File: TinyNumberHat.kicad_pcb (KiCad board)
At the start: 4 copper layers, 65 x 30 mm, 38 parts, among them IC1 SamacSys_Parts_HT16K33-28SOP, J1 GPIO, J2 SM04B-SRSS-TB(LF)(SN), SW1 SW_Omron_B3FS, SW2 SW_Omron_B3FS, SW3 SW_Omron_B3FS, SW4 SW_Omron_B3FS

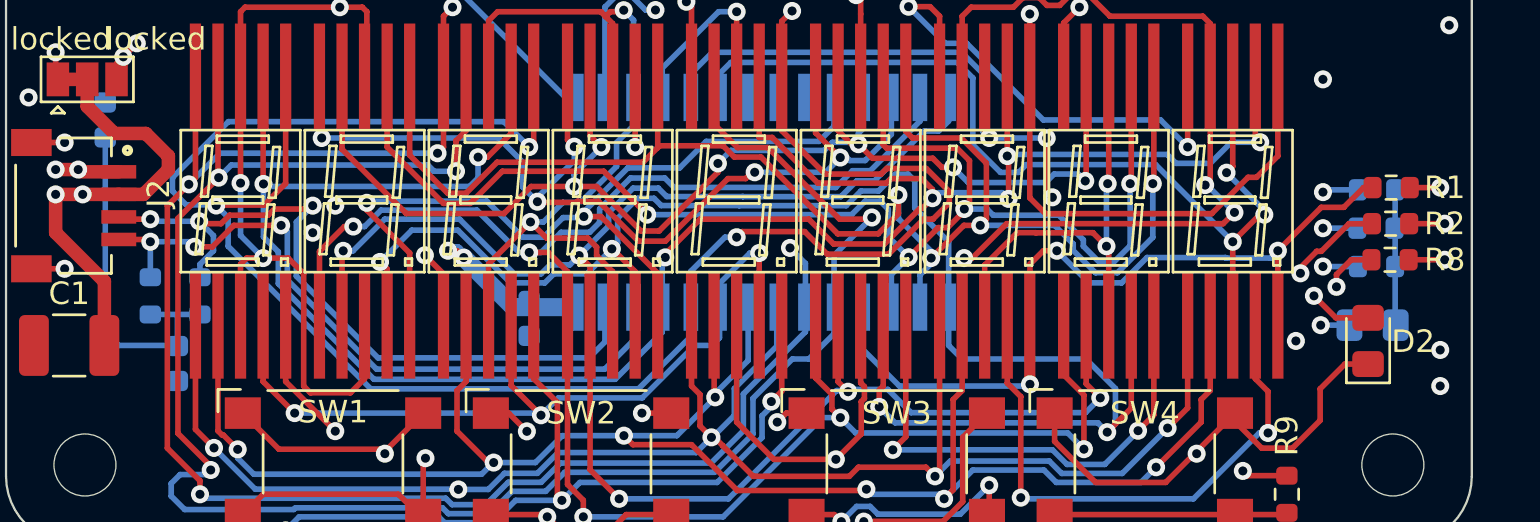
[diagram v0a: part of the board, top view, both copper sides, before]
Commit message: Update silkscreens
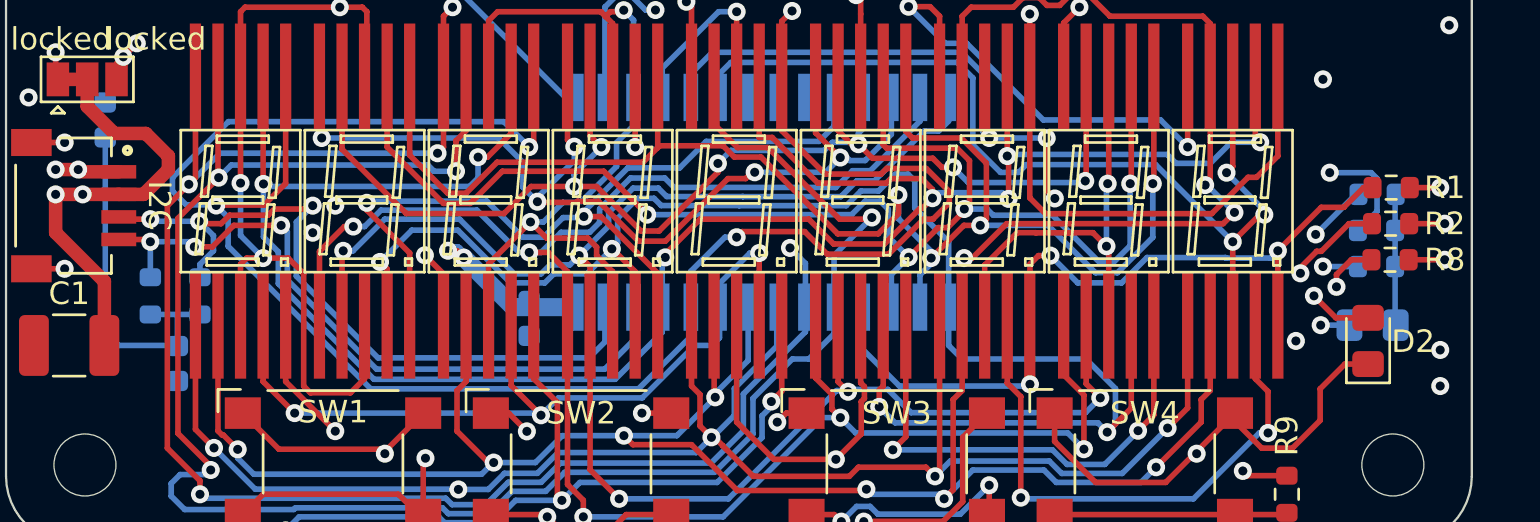
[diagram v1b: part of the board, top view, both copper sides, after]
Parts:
- moved R4 1.80 mm to (160.8, 86.1)
- moved R5 1.50 mm to (160.8, 84.5)
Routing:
- net /an1: track 143.2 -> 146.2 mm
- net /an2: track 97.4 -> 98.1 mm

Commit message: Minor updates
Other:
- board text removed: "Extend PCB edge 0.5mm if using SMT header"
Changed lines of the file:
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@@
     )
   )
-  (footprint "Button_Switch_SMD:SW_SPST_Omron_B3FS-105xP" (layer "F.Cu")
+  (footprint "Button_Switch_SMD:SW_SPST_Omron_B3FS-105xP" locked (layer "F.Cu")
     (at 150.5 96.45)
     (descr "Surface Mount Tactile Switch for High-Density Mounting, 7.3mm height, https://omronfs.omron.com/en_US/ecb/products/pdf/en-b3fs.pdf")
@@
     (fp_circle (center 0 0) (end 1.5 0)
       (stroke (width 0.1) (type solid)) (fill none) (layer "F.Fab"))
-    (pad "1" smd rect (at -4 -2.25 180) (size 1.6 1.4) (layers "F.Cu" "F.Paste" "F.Mask")
+    (pad "1" smd rect locked (at -4 -2.25 180) (size 1.6 1.4) (layers "F.Cu" "F.Paste" "F.Mask")
       (net 32 "Net-(D2-K)") (pinfunction "1") (pintype "passive"))
-    (pad "1" smd rect (at 4 -2.25 180) (size 1.6 1.4) (layers "F.Cu" "F.Paste" "F.Mask")
+    (pad "1" smd rect locked (at 4 -2.25 180) (size 1.6 1.4) (layers "F.Cu" "F.Paste" "F.Mask")
       (net 32 "Net-(D2-K)") (pinfunction "1") (pintype "passive"))
-    (pad "2" smd rect (at -4 2.25 180) (size 1.6 1.4) (layers "F.Cu" "F.Paste" "F.Mask")
+    (pad "2" smd rect locked (at -4 2.25 180) (size 1.6 1.4) (layers "F.Cu" "F.Paste" "F.Mask")
       (net 61 "Net-(R9-Pad1)") (pinfunction "2") (pintype "passive"))
-    (pad "2" smd rect (at 4 2.25 180) (size 1.6 1.4) (layers "F.Cu" "F.Paste" "F.Mask")
+    (pad "2" smd rect locked (at 4 2.25 180) (size 1.6 1.4) (layers "F.Cu" "F.Paste" "F.Mask")
       (net 61 "Net-(R9-Pad1)") (pinfunction "2") (pintype "passive"))
     (model "${KICAD6_3DMODEL_DIR}/Button_Switch_SMD.3dshapes/SW_SPST_Omron_B3FS-105xP.wrl"
@@
     )
   )
-  (footprint "Button_Switch_SMD:SW_SPST_Omron_B3FS-105xP" (layer "F.Cu")
+  (footprint "Button_Switch_SMD:SW_SPST_Omron_B3FS-105xP" locked (layer "F.Cu")
     (at 114.5 96.45)
     (descr "Surface Mount Tactile Switch for High-Density Mounting, 7.3mm height, https://omronfs.omron.com/en_US/ecb/products/pdf/en-b3fs.pdf")
@@
     (fp_circle (center 0 0) (end 1.5 0)
       (stroke (width 0.1) (type solid)) (fill none) (layer "F.Fab"))
-    (pad "1" smd rect (at -4 -2.25 180) (size 1.6 1.4) (layers "F.Cu" "F.Paste" "F.Mask")
+    (pad "1" smd rect locked (at -4 -2.25 180) (size 1.6 1.4) (layers "F.Cu" "F.Paste" "F.Mask")
       (net 32 "Net-(D2-K)") (pinfunction "1") (pintype "passive"))
-    (pad "1" smd rect (at 4 -2.25 180) (size 1.6 1.4) (layers "F.Cu" "F.Paste" "F.Mask")
+    (pad "1" smd rect locked (at 4 -2.25 180) (size 1.6 1.4) (layers "F.Cu" "F.Paste" "F.Mask")
       (net 32 "Net-(D2-K)") (pinfunction "1") (pintype "passive"))
-    (pad "2" smd rect (at -4 2.25 180) (size 1.6 1.4) (layers "F.Cu" "F.Paste" "F.Mask")
+    (pad "2" smd rect locked (at -4 2.25 180) (size 1.6 1.4) (layers "F.Cu" "F.Paste" "F.Mask")
       (net 33 "Net-(R1-Pad1)") (pinfunction "2") (pintype "passive"))
-    (pad "2" smd rect (at 4 2.25 180) (size 1.6 1.4) (layers "F.Cu" "F.Paste" "F.Mask")
+    (pad "2" smd rect locked (at 4 2.25 180) (size 1.6 1.4) (layers "F.Cu" "F.Paste" "F.Mask")
       (net 33 "Net-(R1-Pad1)") (pinfunction "2") (pintype "passive"))
     (model "${KICAD6_3DMODEL_DIR}/Button_Switch_SMD.3dshapes/SW_SPST_Omron_B3FS-105xP.wrl"
@@
     )
   )
-  (footprint "Button_Switch_SMD:SW_SPST_Omron_B3FS-105xP" (layer "F.Cu")
+  (footprint "Button_Switch_SMD:SW_SPST_Omron_B3FS-105xP" locked (layer "F.Cu")
     (at 125.5 96.45)
     (descr "Surface Mount Tactile Switch for High-Density Mounting, 7.3mm height, https://omronfs.omron.com/en_US/ecb/products/pdf/en-b3fs.pdf")
@@
     (fp_circle (center 0 0) (end 1.5 0)
       (stroke (width 0.1) (type solid)) (fill none) (layer "F.Fab"))
-    (pad "1" smd rect (at -4 -2.25 180) (size 1.6 1.4) (layers "F.Cu" "F.Paste" "F.Mask")
+    (pad "1" smd rect locked (at -4 -2.25 180) (size 1.6 1.4) (layers "F.Cu" "F.Paste" "F.Mask")
       (net 32 "Net-(D2-K)") (pinfunction "1") (pintype "passive"))
-    (pad "1" smd rect (at 4 -2.25 180) (size 1.6 1.4) (layers "F.Cu" "F.Paste" "F.Mask")
+    (pad "1" smd rect locked (at 4 -2.25 180) (size 1.6 1.4) (layers "F.Cu" "F.Paste" "F.Mask")
       (net 32 "Net-(D2-K)") (pinfunction "1") (pintype "passive"))
-    (pad "2" smd rect (at -4 2.25 180) (size 1.6 1.4) (layers "F.Cu" "F.Paste" "F.Mask")
+    (pad "2" smd rect locked (at -4 2.25 180) (size 1.6 1.4) (layers "F.Cu" "F.Paste" "F.Mask")
       (net 34 "Net-(R2-Pad1)") (pinfunction "2") (pintype "passive"))
-    (pad "2" smd rect (at 4 2.25 180) (size 1.6 1.4) (layers "F.Cu" "F.Paste" "F.Mask")
+    (pad "2" smd rect locked (at 4 2.25 180) (size 1.6 1.4) (layers "F.Cu" "F.Paste" "F.Mask")
       (net 34 "Net-(R2-Pad1)") (pinfunction "2") (pintype "passive"))
     (model "${KICAD6_3DMODEL_DIR}/Button_Switch_SMD.3dshapes/SW_SPST_Omron_B3FS-105xP.wrl"
@@
     (effects (font (size 1 1) (thickness 0.15)) (justify left bottom))
   )
-  (gr_text "Extend PCB edge 0.5mm if using SMT header" (at 103 68.5) (layer "Dwgs.User")
-    (effects (font (size 1 1) (thickness 0.15)) (justify left))
-  )
   (gr_text "PoE" (at 161.5 79.64) (layer "Dwgs.User")

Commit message: Small updates
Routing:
- net /an5: track 123.9 -> 131.1 mm
- net /an13: track 61.5 -> 58.8 mm
- net /an1: track 146.2 -> 145.1 mm
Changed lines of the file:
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@@
   (via (at 145.4 76.5) (size 0.8) (drill 0.4) (layers "F.Cu" "B.Cu") (net 38))
   (via (at 132.4 86.4) (size 0.8) (drill 0.4) (layers "F.Cu" "B.Cu") (net 38))
-  (segment (start 137.845403 77.4) (end 135.889999 77.4) (width 0.25) (layer "In1.Cu") (net 38))
   (segment (start 156.362079 81.2) (end 150.1 81.2) (width 0.25) (layer "In1.Cu") (net 38))
   (segment (start 158.7 83.537921) (end 156.362079 81.2) (width 0.25) (layer "In1.Cu") (net 38))
-  (segment (start 145.4 76.5) (end 141.3 76.5) (width 0.25) (layer "In1.Cu") (net 38))
-  (segment (start 139.858434 75.386969) (end 137.845403 77.4) (width 0.25) (layer "In1.Cu") (net 38))
-  (segment (start 135.889999 77.4) (end 134.857326 76.367327) (width 0.25) (layer "In1.Cu") (net 38))
-  (segment (start 141.3 76.5) (end 140.186969 75.386969) (width 0.25) (layer "In1.Cu") (net 38))
-  (segment (start 140.186969 75.386969) (end 139.858434 75.386969) (width 0.25) (layer "In1.Cu") (net 38))
+  (segment (start 144.7 77.2) (end 135.689999 77.2) (width 0.25) (layer "In1.Cu") (net 38))
+  (segment (start 135.689999 77.2) (end 134.857326 76.367327) (width 0.25) (layer "In1.Cu") (net 38))
+  (segment (start 145.4 76.5) (end 144.7 77.2) (width 0.25) (layer "In1.Cu") (net 38))
   (segment (start 150.1 81.2) (end 145.4 76.5) (width 0.25) (layer "In1.Cu") (net 38))
   (segment (start 160.8 83.8) (end 160.8 85.25) (width 0.25) (layer "B.Cu") (net 38))
@@
   (segment (start 153.4 83.863381) (end 153.175467 84.087914) (width 0.25) (layer "F.Cu") (net 44))
   (segment (start 153.975 85.8) (end 154.475 85.3) (width 0.25) (layer "F.Cu") (net 44))
-  (segment (start 147.320405 75.525) (end 147.879595 75.525) (width 0.25) (layer "F.Cu") (net 44))
+  (segment (start 146.639946 76.6) (end 153.075 76.6) (width 0.25) (layer "F.Cu") (net 44))
   (segment (start 138.395443 85.525907) (end 138.32135 85.6) (width 0.25) (layer "F.Cu") (net 44))
-  (segment (start 145.099695 75.775) (end 145.814946 75.775) (width 0.25) (layer "F.Cu") (net 44))
-  (segment (start 142.4 79.3) (end 142.4 76.6) (width 0.25) (layer "F.Cu") (net 44))
+  (segment (start 144.674695 76.2) (end 145.099695 75.775) (width 0.25) (layer "F.Cu") (net 44))
   (segment (start 136.963604 85.6) (end 133.788604 82.425) (width 0.25) (layer "F.Cu") (net 44))
   (segment (start 120.4 81.675) (end 119.954623 82.120377) (width 0.25) (layer "F.Cu") (net 44))
-  (segment (start 153.4 76.925) (end 153.4 79.3) (width 0.25) (layer "F.Cu") (net 44))
   (segment (start 144.37245 85.8) (end 153.975 85.8) (width 0.25) (layer "F.Cu") (net 44))
-  (segment (start 146.160351 76.120405) (end 146.725 76.120405) (width 0.25) (layer "F.Cu") (net 44))
-  (segment (start 148.954595 76.6) (end 153.075 76.6) (width 0.25) (layer "F.Cu") (net 44))
-  (segment (start 145.814946 75.775) (end 146.160351 76.120405) (width 0.25) (layer "F.Cu") (net 44))
+  (segment (start 153.075 76.6) (end 153.4 76.925) (width 0.25) (layer "F.Cu") (net 44))
+  (segment (start 145.099695 75.775) (end 145.814946 75.775) (width 0.25) (layer "F.Cu") (net 44))
   (segment (start 142.8 76.2) (end 144.674695 76.2) (width 0.25) (layer "F.Cu") (net 44))
   (segment (start 131.4 81.38462) (end 131.4 79.3) (width 0.25) (layer "F.Cu") (net 44))
@@
   (segment (start 138.32135 85.6) (end 136.963604 85.6) (width 0.25) (layer "F.Cu") (net 44))
   (segment (start 119.954623 82.120377) (end 119.954623 83.475) (width 0.25) (layer "F.Cu") (net 44))
+  (segment (start 142.4 76.6) (end 142.8 76.2) (width 0.25) (layer "F.Cu") (net 44))
   (segment (start 142.84745 87.325) (end 144.37245 85.8) (width 0.25) (layer "F.Cu") (net 44))
   (segment (start 142.486661 87.325) (end 142.84745 87.325) (width 0.25) (layer "F.Cu") (net 44))
-  (segment (start 147.879595 75.525) (end 148.954595 76.6) (width 0.25) (layer "F.Cu") (net 44))
-  (segment (start 153.075 76.6) (end 153.4 76.925) (width 0.25) (layer "F.Cu") (net 44))
   (segment (start 120.4 79.3) (end 120.4 81.675) (width 0.25) (layer "F.Cu") (net 44))
   (segment (start 107.624062 95.099122) (end 109.077298 96.552358) (width 0.25) (layer "F.Cu") (net 44))
@@
   (segment (start 109.4 83.72762) (end 109.429853 83.757473) (width 0.25) (layer "F.Cu") (net 44))
   (segment (start 132.44038 82.425) (end 131.4 81.38462) (width 0.25) (layer "F.Cu") (net 44))
-  (segment (start 146.725 76.120405) (end 147.320405 75.525) (width 0.25) (layer "F.Cu") (net 44))
-  (segment (start 142.4 76.6) (end 142.8 76.2) (width 0.25) (layer "F.Cu") (net 44))
+  (segment (start 145.814946 75.775) (end 146.639946 76.6) (width 0.25) (layer "F.Cu") (net 44))
+  (segment (start 142.4 79.3) (end 142.4 76.6) (width 0.25) (layer "F.Cu") (net 44))
   (segment (start 107.624062 85.563264) (end 107.624062 95.099122) (width 0.25) (layer "F.Cu") (net 44))
   (segment (start 133.788604 82.425) (end 132.44038 82.425) (width 0.25) (layer "F.Cu") (net 44))
-  (segment (start 144.674695 76.2) (end 145.099695 75.775) (width 0.25) (layer "F.Cu") (net 44))
   (segment (start 109.429853 83.757473) (end 107.624062 85.563264) (width 0.25) (layer "F.Cu") (net 44))
   (segment (start 109.4 79.3) (end 109.4 83.72762) (width 0.25) (layer "F.Cu") (net 44))
+  (segment (start 153.4 76.925) (end 153.4 79.3) (width 0.25) (layer "F.Cu") (net 44))
   (via (at 119.954623 83.475) (size 0.8) (drill 0.4) (layers "F.Cu" "B.Cu") (net 44))
   (via (at 142.486661 87.325) (size 0.8) (drill 0.4) (layers "F.Cu" "B.Cu") (net 44))
@@
   (via (at 140.022701 76.177297) (size 0.8) (drill 0.4) (layers "F.Cu" "B.Cu") (net 45))
   (segment (start 134.765702 86.875) (end 140.8 80.840702) (width 0.25) (layer "In1.Cu") (net 45))
+  (segment (start 149.175016 80.840702) (end 150.734314 82.4) (width 0.25) (layer "In1.Cu") (net 45))
   (segment (start 121.008235 77.408235) (end 119.8 76.2) (width 0.25) (layer "In1.Cu") (net 45))
-  (segment (start 140.8 76.954596) (end 140.022701 76.177297) (width 0.25) (layer "In1.Cu") (net 45))
+  (segment (start 140.8 80.840702) (end 149.175016 80.840702) (width 0.25) (layer "In1.Cu") (net 45))
   (segment (start 128.719374 77.408235) (end 121.008235 77.408235) (width 0.25) (layer "In1.Cu") (net 45))
-  (segment (start 140.8 80.840702) (end 140.8 76.954596) (width 0.25) (layer "In1.Cu") (net 45))
+  (segment (start 150.734314 82.4) (end 152.4 82.4) (width 0.25) (layer "In1.Cu") (net 45))
   (segment (start 130.170145 75.957464) (end 128.719374 77.408235) (width 0.25) (layer "In1.Cu") (net 45))
   (segment (start 123.73012 97.26988) (end 122.268395 97.26988) (width 0.25) (layer "B.Cu") (net 45))
@@
   (segment (start 125.299874 84.854721) (end 123.592861 84.854721) (width 0.25) (layer "F.Cu") (net 60))
   (segment (start 135.9 79.3) (end 135.9 81.77137) (width 0.25) (layer "F.Cu") (net 60))
-  (segment (start 147.6 76.1995) (end 146.9 76.8995) (width 0.25) (layer "F.Cu") (net 60))
   (segment (start 128.041901 86.575002) (end 126.276483 84.809584) (width 0.25) (layer "F.Cu") (net 60))
   (segment (start 113.9 79.3) (end 113.9 81.89999) (width 0.25) (layer "F.Cu") (net 60))
+  (segment (start 146.9 81.858099) (end 146.9 79.3) (width 0.25) (layer "F.Cu") (net 60))
   (segment (start 123.592861 84.854721) (end 123.563802 84.825662) (width 0.25) (layer "F.Cu") (net 60))
-  (segment (start 146.9 76.8995) (end 146.9 79.3) (width 0.25) (layer "F.Cu") (net 60))
   (segment (start 126.276483 84.809584) (end 125.345011 84.809584) (width 0.25) (layer "F.Cu") (net 60))
+  (segment (start 147.097816 82.055915) (end 146.9 81.858099) (width 0.25) (layer "F.Cu") (net 60))
   (segment (start 132.014168 83.8) (end 129.239166 86.575002) (width 0.25) (layer "F.Cu") (net 60))
   (segment (start 133.080033 83.519967) (end 132.8 83.8) (width 0.25) (layer "F.Cu") (net 60))
@@
   (via (at 123.563802 84.825662) (size 0.8) (drill 0.4) (layers "F.Cu" "B.Cu") (net 60))
   (via (at 136.995166 82.866536) (size 0.8) (drill 0.4) (layers "F.Cu" "B.Cu") (net 60))
-  (via (at 147.6 76.1995) (size 0.8) (drill 0.4) (layers "F.Cu" "B.Cu") (net 60))
+  (via (at 147.097816 82.055915) (size 0.8) (drill 0.4) (layers "F.Cu" "B.Cu") (net 60))
   (via (at 125.200004 82.385439) (size 0.8) (drill 0.4) (layers "F.Cu" "B.Cu") (net 60))
+  (segment (start 137.07813 82.9495) (end 136.995166 82.866536) (width 0.25) (layer "In2.Cu") (net 60))
+  (segment (start 142.4745 81.325) (end 140.85 82.9495) (width 0.25) (layer "In2.Cu") (net 60))
+  (segment (start 146.824773 81.72582) (end 146.423953 81.325) (width 0.25) (layer "In2.Cu") (net 60))
+  (segment (start 146.824773 82.055915) (end 146.824773 81.72582) (width 0.25) (layer "In2.Cu") (net 60))
   (segment (start 140.85 82.9495) (end 137.07813 82.9495) (width 0.25) (layer "In2.Cu") (net 60))
-  (segment (start 137.07813 82.9495) (end 136.995166 82.866536) (width 0.25) (layer "In2.Cu") (net 60))
-  (segment (start 147.6 76.1995) (end 140.85 82.9495) (width 0.25) (layer "In2.Cu") (net 60))
+  (segment (start 147.097816 82.055915) (end 146.824773 82.055915) (width 0.25) (layer "In2.Cu") (net 60))
+  (segment (start 146.423953 81.325) (end 142.4745 81.325) (width 0.25) (layer "In2.Cu") (net 60))
   (segment (start 125.200004 82.385439) (end 125.200004 82.999996) (width 0.25) (layer "B.Cu") (net 60))
   (segment (start 121.845395 81.99999) (end 122.920405 83.075) (width 0.25) (layer "B.Cu") (net 60))
